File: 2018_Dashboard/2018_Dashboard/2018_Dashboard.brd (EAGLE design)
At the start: 127 x 58.4 mm, 51 parts, among them Y1 16MHz

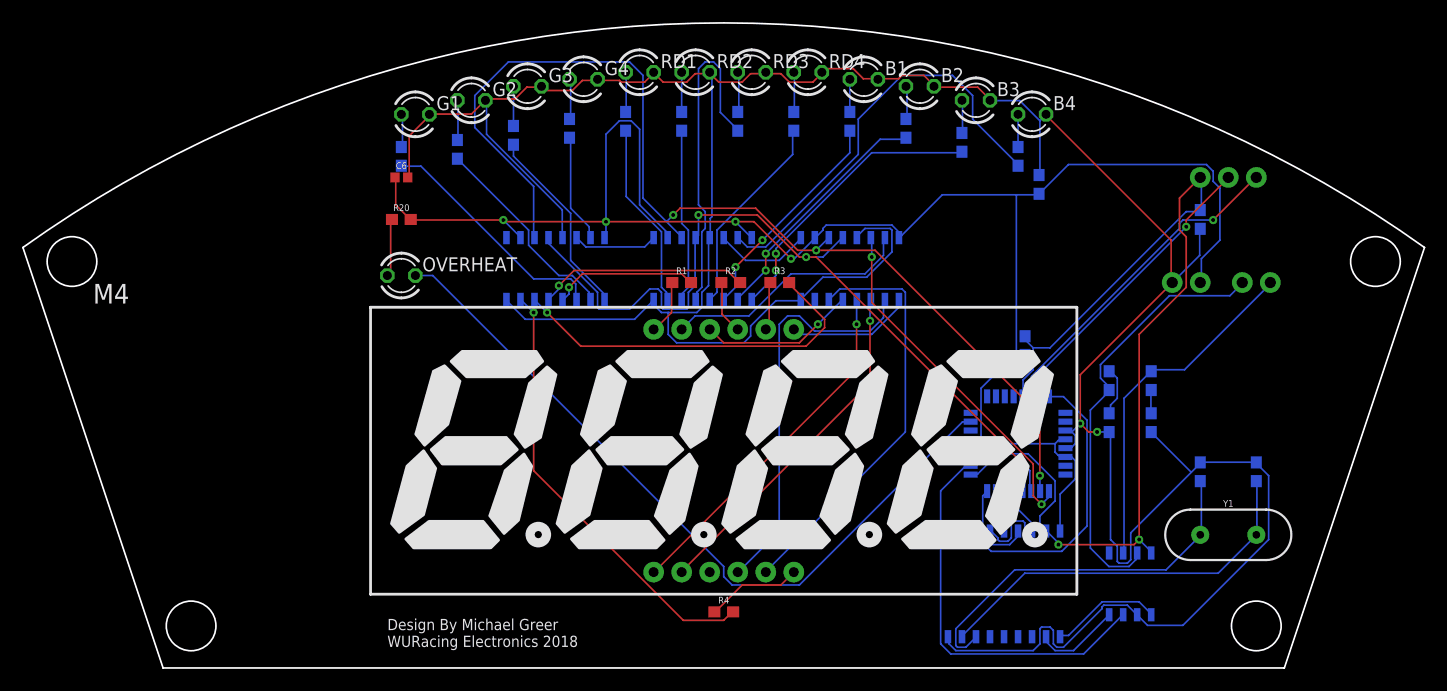
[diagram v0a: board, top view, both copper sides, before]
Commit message: Post order changes for 2019 car: Made board more narrow Added breakout headers for buring bootloader git commit -m
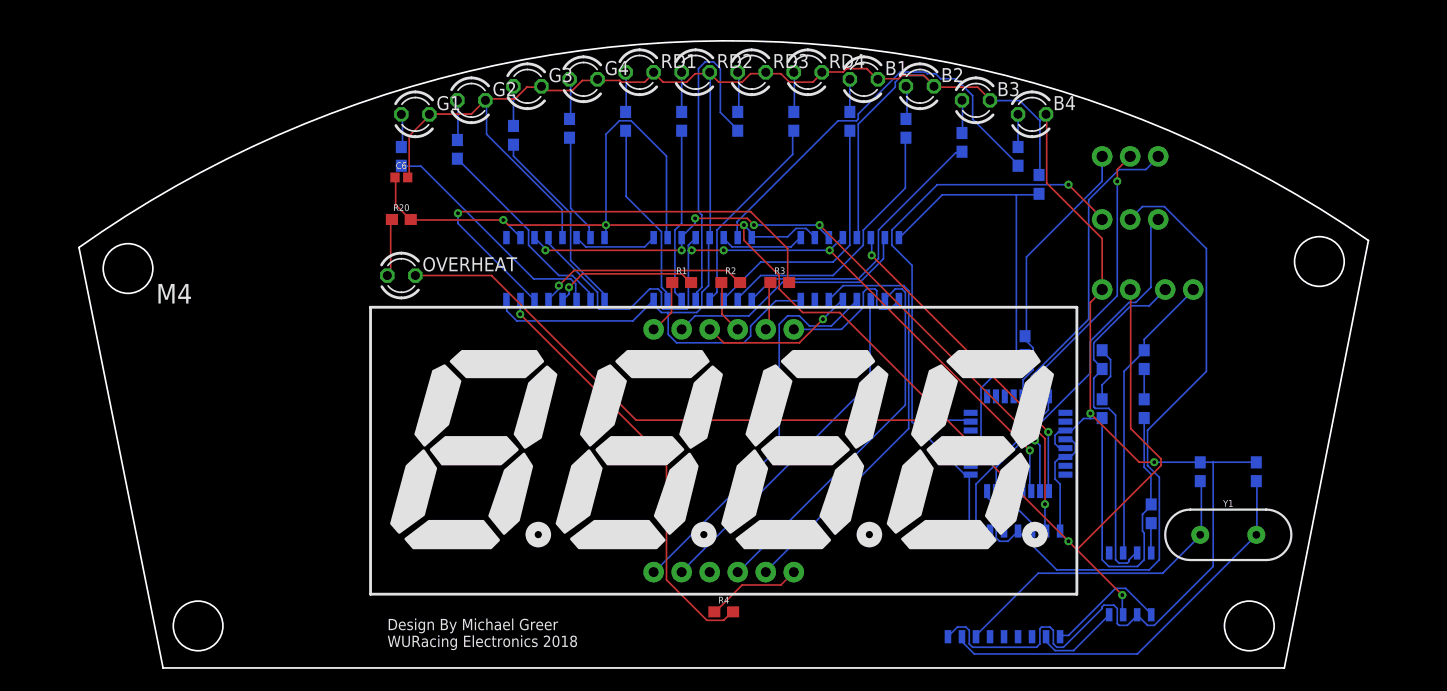
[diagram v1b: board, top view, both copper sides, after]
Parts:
- added BOOTLOADER: (no value), SparkFun-Connectors:1X03
- PROGRAM: value 455-1750-1-ND -> (none)
- moved R22 27.0 mm to (80.6, 31.8), turned to 270 degrees
- moved PROGRAM 9.09 mm to (81.3, 64.1)
- moved CAN 7.01 mm to (84.5, 52.1)
- moved POWER 6.38 mm to (78.7, 52.1)
- moved CANH 2.01 mm to (76.2, 45.7)
- moved CANL 2.01 mm to (80.0, 45.7)
- moved C4 1.42 mm to (76.2, 41.3)
- moved C5 1.42 mm to (80.0, 41.3)
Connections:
- net N$67 renamed RX
- net N$68 renamed TX
- removed net N$53: CAN_SERIAL.14, CONTROL.15
- removed net N$54: CAN_SERIAL.15, CONTROL.16
- removed net N$55: CAN_SERIAL.13, CONTROL.17
- removed net N$61: CAN_INTERFACE.8, CAN_SERIAL.17, CONTROL.29, PROGRAM.3, R21.2, R22.2
- new net MISO: BOOTLOADER.2, CAN_SERIAL.15, CONTROL.16
- new net MOSI: BOOTLOADER.1, CAN_SERIAL.14, CONTROL.15
- new net N$1: CAN_INTERFACE.8, R22.2
- new net RST: CAN_SERIAL.17, CONTROL.29, PROGRAM.3, R21.2
- new net SCK: BOOTLOADER.3, CAN_SERIAL.13, CONTROL.17
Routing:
- net N$61: track 76.1 -> 0.00 mm, vias 2 -> 0
- net MISO: track 0.00 -> 61.5 mm
- net SCK: track 0.00 -> 55.7 mm, vias 0 -> 1
- net RST: track 0.00 -> 38.5 mm, vias 0 -> 2
- net N$21: track 98.9 -> 62.7 mm, vias 3 -> 6
- net MOSI: track 0.00 -> 35.0 mm
- net N$55: track 23.4 -> 0.00 mm
- net N$51: track 68.6 -> 55.8 mm, vias 0 -> 1
- net N$5: track 34.2 -> 45.2 mm
- net N$56: track 26.0 -> 15.0 mm
- net N$54: track 8.64 -> 0.00 mm
- net CANH: track 39.4 -> 32.9 mm
- net N$59: track 34.5 -> 29.2 mm
- net CANL: track 31.7 -> 26.5 mm
- net N$53: track 3.91 -> 0.00 mm
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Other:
- board size 127 x 58.4 mm -> 116.8 x 56.8 mm
- board text added: "CANH"
- board text added: "CANL"
- board text added: "GND"
- board text added: "MISO"
- board text added: "MOSI"
- board text added: "RST"
- board text added: "RX"
- board text added: "SCK"
- board text added: "TX"
- board text added: "VCC"
